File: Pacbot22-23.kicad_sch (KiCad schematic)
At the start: 8 parts, among them SW1 SW_Push, U1 ATmega32U4-A, Y1 16Mhz

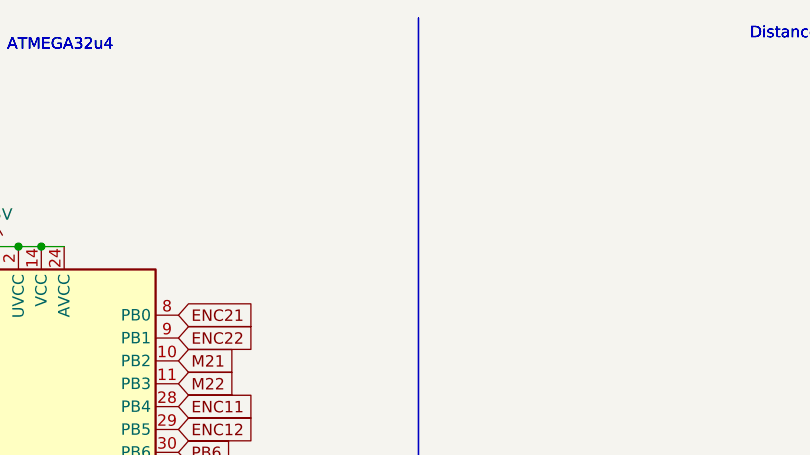
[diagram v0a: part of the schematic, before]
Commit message: Added bluetooth schematic lmao my b for not putting this on the original
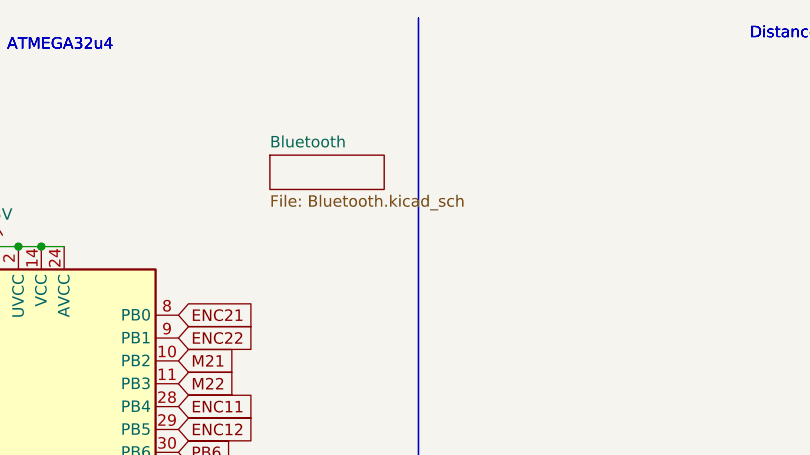
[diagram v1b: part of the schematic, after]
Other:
- added sheet Bluetooth (Bluetooth.kicad_sch)
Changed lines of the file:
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@@
+    (stroke (width 0) (type default) (color 0 0 0 0))
+  )
+  (polyline (pts (xy 176.53 71.12) (xy 234.95 71.12))
     (stroke (width 0) (type default) (color 0 0 0 0))
   )
@@
     (stroke (width 0) (type default) (color 0 0 0 0))
   )
+  (polyline (pts (xy 234.95 71.12) (xy 284.48 71.12))
+    (stroke (width 0) (type default) (color 0 0 0 0))
+  )
   (polyline (pts (xy 110.49 142.24) (xy 110.49 198.12))
     (stroke (width 0) (type default) (color 0 0 0 0))
   )
+  (polyline (pts (xy 110.49 142.24) (xy 110.49 198.12))
+    (stroke (width 0) (type default) (color 0 0 0 0))
+  )
   (polyline (pts (xy 110.49 142.24) (xy 176.53 142.24))
     (stroke (width 0) (type default) (color 0 0 0 0))
   )
+  (polyline (pts (xy 110.49 142.24) (xy 176.53 142.24))
+    (stroke (width 0) (type default) (color 0 0 0 0))
+  )
   (wire (pts (xy 78.74 93.98) (xy 85.09 93.98))
     (stroke (width 0) (type default) (color 0 0 0 0))
@@
     (stroke (width 0) (type default) (color 0 0 0 0))
   )
+  (polyline (pts (xy 176.53 113.03) (xy 284.48 113.03))
+    (stroke (width 0) (type default) (color 0 0 0 0))
+  )
   (polyline (pts (xy 88.9 142.24) (xy 110.49 142.24))
     (stroke (width 0) (type default) (color 0 0 0 0))
   )
+  (polyline (pts (xy 88.9 142.24) (xy 110.49 142.24))
+    (stroke (width 0) (type default) (color 0 0 0 0))
+  )
   (wire (pts (xy 41.91 129.54) (xy 44.45 129.54))
     (stroke (width 0) (type default) (color 0 0 0 0))
@@
     (stroke (width 0) (type default) (color 0 0 0 0))
   )
+  (polyline (pts (xy 12.7 142.24) (xy 88.9 142.24))
+    (stroke (width 0) (type default) (color 0 0 0 0))
+  )
   (wire (pts (xy 62.23 99.06) (xy 68.58 99.06))
     (stroke (width 0) (type default) (color 0 0 0 0))
@@
     (stroke (width 0) (type default) (color 0 0 0 0))
   )
+  (polyline (pts (xy 88.9 12.7) (xy 88.9 142.24))
+    (stroke (width 0) (type default) (color 0 0 0 0))
+  )
   (wire (pts (xy 16.51 50.8) (xy 16.51 55.88))
     (stroke (width 0) (type default) (color 0 0 0 0))
@@
     (stroke (width 0) (type default) (color 0 0 0 0))
   )
+  (polyline (pts (xy 176.53 142.24) (xy 176.53 166.37))
+    (stroke (width 0) (type default) (color 0 0 0 0))
+  )
   (polyline (pts (xy 12.7 181.61) (xy 50.8 181.61))
     (stroke (width 0) (type default) (color 0 0 0 0))
   )
+  (polyline (pts (xy 12.7 181.61) (xy 50.8 181.61))
+    (stroke (width 0) (type default) (color 0 0 0 0))
+  )
   (wire (pts (xy 44.45 129.54) (xy 46.99 129.54))
     (stroke (width 0) (type default) (color 0 0 0 0))
@@
     (stroke (width 0) (type default) (color 0 0 0 0))
   )
+  (polyline (pts (xy 50.8 142.24) (xy 50.8 198.12))
+    (stroke (width 0) (type default) (color 0 0 0 0))
+  )
   (polyline (pts (xy 176.53 12.7) (xy 176.53 142.24))
     (stroke (width 0) (type default) (color 0 0 0 0))
   )
+  (polyline (pts (xy 176.53 12.7) (xy 176.53 142.24))
+    (stroke (width 0) (type default) (color 0 0 0 0))
+  )
   (wire (pts (xy 44.45 38.1) (xy 46.99 38.1))
     (stroke (width 0) (type default) (color 0 0 0 0))
@@
     (effects (font (size 1.27 1.27)) (justify left bottom))
   )
+  (text "ATMEGA32u4" (at 43.18 16.51 0)
+    (effects (font (size 1.27 1.27)) (justify left bottom))
+  )
   (text "Shift Reg" (at 228.6 76.2 0)
     (effects (font (size 1.27 1.27)) (justify left bottom))
   )
+  (text "Shift Reg" (at 228.6 76.2 0)
+    (effects (font (size 1.27 1.27)) (justify left bottom))
+  )
   (text "USB Connector" (at 22.86 147.32 0)
     (effects (font (size 1.27 1.27)) (justify left bottom))
   )
+  (text "USB Connector" (at 22.86 147.32 0)
+    (effects (font (size 1.27 1.27)) (justify left bottom))
+  )
   (text "Power Term" (at 24.13 184.15 0)
     (effects (font (size 1.27 1.27)) (justify left bottom))
   )
+  (text "Power Term" (at 24.13 184.15 0)
+    (effects (font (size 1.27 1.27)) (justify left bottom))
+  )
   (text "H-Bridges" (at 227.33 115.57 0)
     (effects (font (size 1.27 1.27)) (justify left bottom))
   )
+  (text "H-Bridges" (at 227.33 115.57 0)
+    (effects (font (size 1.27 1.27)) (justify left bottom))
+  )
   (text "BNO055 IMU" (at 73.66 147.32 0)
     (effects (font (size 1.27 1.27)) (justify left bottom))
   )
+  (text "BNO055 IMU" (at 73.66 147.32 0)
+    (effects (font (size 1.27 1.27)) (justify left bottom))
+  )
   (text "Distance Sensors" (at 125.73 15.24 0)
     (effects (font (size 1.27 1.27)) (justify left bottom))
   )
+  (text "Distance Sensors" (at 125.73 15.24 0)
+    (effects (font (size 1.27 1.27)) (justify left bottom))
+  )
   (text "Decoupling Capacitors" (at 222.25 15.24 0)
+    (effects (font (size 1.27 1.27)) (justify left bottom))
+  )
+  (text "Decoupling Capacitors" (at 222.25 15.24 0)
+    (effects (font (size 1.27 1.27)) (justify left bottom))
+  )
+  (text "Motor Connectors" (at 137.16 147.32 0)
     (effects (font (size 1.27 1.27)) (justify left bottom))
   )
@@
     (pin "1")
   )
+  (sheet (at 72.39 27.94) (size 12.7 3.81) (fields_autoplaced)
+    (stroke (width 0.1524) (type solid) (color 0 0 0 0))
+    (fill (color 0 0 0 0.0000))
+    (property "Sheet name" "Bluetooth" (id 0) (at 72.39 27.2284 0)
+      (effects (font (size 1.27 1.27)) (justify left bottom))
+    )
+    (property "Sheet file" "Bluetooth.kicad_sch" (id 1) (at 72.39 32.3346 0)
+      (effects (font (size 1.27 1.27)) (justify left top))
+    )
+  )
   (sheet (at 13.97 132.08) (size 12.7 3.81) (fields_autoplaced)
     (stroke (width 0.1524) (type solid) (color 0 0 0 0))
@@
     )
   )
-  (polyline (pts (xy 176.53 71.12) (xy 234.95 71.12))
-    (stroke (width 0) (type default) (color 0 0 0 0))
-  )
-  (polyline (pts (xy 234.95 71.12) (xy 284.48 71.12))
-    (stroke (width 0) (type default) (color 0 0 0 0))
-  )
-  (polyline (pts (xy 110.49 142.24) (xy 110.49 198.12))
-    (stroke (width 0) (type default) (color 0 0 0 0))
-  )
-  (polyline (pts (xy 110.49 142.24) (xy 176.53 142.24))
-    (stroke (width 0) (type default) (color 0 0 0 0))
-  )
-  (polyline (pts (xy 176.53 113.03) (xy 284.48 113.03))
-    (stroke (width 0) (type default) (color 0 0 0 0))
-  )
-  (polyline (pts (xy 88.9 142.24) (xy 110.49 142.24))
-    (stroke (width 0) (type default) (color 0 0 0 0))
-  )
-  (polyline (pts (xy 12.7 142.24) (xy 88.9 142.24))
-    (stroke (width 0) (type default) (color 0 0 0 0))
-  )
-  (polyline (pts (xy 88.9 12.7) (xy 88.9 142.24))
-    (stroke (width 0) (type default) (color 0 0 0 0))
-  )
-  (polyline (pts (xy 176.53 142.24) (xy 176.53 166.37))
-    (stroke (width 0) (type default) (color 0 0 0 0))
-  )
-  (polyline (pts (xy 12.7 181.61) (xy 50.8 181.61))
-    (stroke (width 0) (type default) (color 0 0 0 0))
-  )
-  (polyline (pts (xy 50.8 142.24) (xy 50.8 198.12))
-    (stroke (width 0) (type default) (color 0 0 0 0))
-  )
-  (polyline (pts (xy 176.53 12.7) (xy 176.53 142.24))
-    (stroke (width 0) (type default) (color 0 0 0 0))
-  )
-  (text "ATMEGA32u4" (at 43.18 16.51 0)
-    (effects (font (size 1.27 1.27)) (justify left bottom))
-  )
-  (text "Shift Reg" (at 228.6 76.2 0)
-    (effects (font (size 1.27 1.27)) (justify left bottom))
-  )
-  (text "USB Connector" (at 22.86 147.32 0)
-    (effects (font (size 1.27 1.27)) (justify left bottom))
-  )
-  (text "Power Term" (at 24.13 184.15 0)
-    (effects (font (size 1.27 1.27)) (justify left bottom))
-  )
-  (text "H-Bridges" (at 227.33 115.57 0)
-    (effects (font (size 1.27 1.27)) (justify left bottom))
-  )
-  (text "BNO055 IMU" (at 73.66 147.32 0)
-    (effects (font (size 1.27 1.27)) (justify left bottom))
-  )
-  (text "Distance Sensors" (at 125.73 15.24 0)
-    (effects (font (size 1.27 1.27)) (justify left bottom))
-  )
-  (text "Decoupling Capacitors" (at 222.25 15.24 0)
-    (effects (font (size 1.27 1.27)) (justify left bottom))
-  )
-  (text "Motor Connectors" (at 137.16 147.32 0)
-    (effects (font (size 1.27 1.27)) (justify left bottom))
-  )
   (sheet_instances
     (path "/" (page "1"))
     (path "/590a5ee8-978b-43ec-b66a-3ea6e6e9d751" (page "2"))
+    (path "/4c040f2f-fa7f-436a-8faf-9b6a0a50ff47" (page "3"))
   )
   (symbol_instances
+    (path "/4c040f2f-fa7f-436a-8faf-9b6a0a50ff47/1235810c-b41b-4ed0-bd20-969bf45f4c5d"
+      (reference "#PWR?") (unit 1) (value "+5V") (footprint "")
+    )
     (path "/3c0a01b7-4e1b-44d8-bdba-30f1191e0e18"
       (reference "#PWR?") (unit 1) (value "GND") (footprint "")
@@
       (reference "#PWR?") (unit 1) (value "+5V") (footprint "")
     )
+    (path "/4c040f2f-fa7f-436a-8faf-9b6a0a50ff47/7fa139b8-9215-4d8d-b8f6-47bf890e7075"
+      (reference "#PWR?") (unit 1) (value "GND") (footprint "")
+    )
     (path "/7fb65cb0-26d4-43cc-a7eb-8bd5a42d0ad2"
       (reference "#PWR?") (unit 1) (value "+5V") (footprint "")
@@
       (reference "C10") (unit 1) (value "1uF") (footprint "")
     )
+    (path "/4c040f2f-fa7f-436a-8faf-9b6a0a50ff47/2f3e5db4-814e-49e7-9df2-328f7ec40bd7"
+      (reference "J?") (unit 1) (value "HC-05") (footprint "")
+    )
     (path "/c1671872-1d10-42a0-be49-f152cf9a6c5b"
       (reference "R10") (unit 1) (value "10k") (footprint "")
@@
       (reference "R20") (unit 1) (value "10k") (footprint "")
     )
+    (path "/4c040f2f-fa7f-436a-8faf-9b6a0a50ff47/71a24c17-86c0-4f2a-9098-218d0856092e"
+      (reference "R?") (unit 1) (value "100r") (footprint "")
+    )
     (path "/d23bc10b-7b30-45e0-be45-9461d6acd6cc"

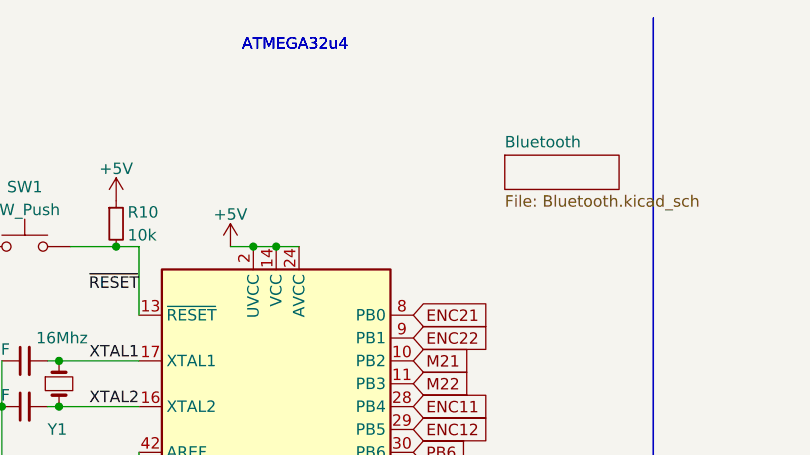
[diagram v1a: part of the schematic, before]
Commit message: Added LVR
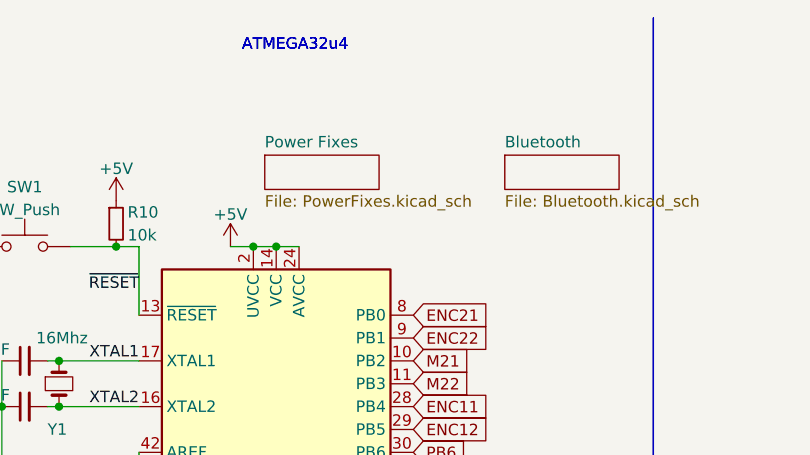
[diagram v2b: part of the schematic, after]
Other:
- added sheet Power Fixes (PowerFixes.kicad_sch)
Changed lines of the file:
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@@
     (pin "1")
+  )
+  (sheet (at 45.72 27.94) (size 12.7 3.81) (fields_autoplaced)
+    (stroke (width 0.1524) (type solid) (color 0 0 0 0))
+    (fill (color 0 0 0 0.0000))
+    (property "Sheet name" "Power Fixes" (id 0) (at 45.72 27.2284 0)
+      (effects (font (size 1.27 1.27)) (justify left bottom))
+    )
+    (property "Sheet file" "PowerFixes.kicad_sch" (id 1) (at 45.72 32.3346 0)
+      (effects (font (size 1.27 1.27)) (justify left top))
+    )
   )
   (sheet (at 72.39 27.94) (size 12.7 3.81) (fields_autoplaced)
@@
     (path "/590a5ee8-978b-43ec-b66a-3ea6e6e9d751" (page "2"))
     (path "/4c040f2f-fa7f-436a-8faf-9b6a0a50ff47" (page "3"))
+    (path "/00edbbb4-cd26-461b-b990-f87a8e329c1c" (page "4"))
   )
   (symbol_instances
@@
       (reference "#PWR?") (unit 1) (value "GND") (footprint "")
     )
+    (path "/00edbbb4-cd26-461b-b990-f87a8e329c1c/4767fd76-6b58-4859-b099-fd1c871601c5"
+      (reference "#PWR?") (unit 1) (value "+5V") (footprint "")
+    )
     (path "/583201a5-9f01-499a-806a-a1c99ed66b6c"
       (reference "#PWR?") (unit 1) (value "GND") (footprint "")
@@
     (path "/a9419ac5-56dd-48db-9f7a-b4183b1c6a1c"
       (reference "#PWR?") (unit 1) (value "GND") (footprint "")
+    )
+    (path "/00edbbb4-cd26-461b-b990-f87a8e329c1c/cfeb6c6d-8f20-41a8-a483-a658024a3995"
+      (reference "#PWR?") (unit 1) (value "+8V") (footprint "")
     )
     (path "/dbabece7-cfc2-4b30-bd49-2b0169e2eb13"
@@
       (reference "C10") (unit 1) (value "1uF") (footprint "")
     )
+    (path "/00edbbb4-cd26-461b-b990-f87a8e329c1c/3720c41d-9d7a-47a6-8680-7f74645e7d2f"
+      (reference "C?") (unit 1) (value "10uF") (footprint "")
+    )
+    (path "/00edbbb4-cd26-461b-b990-f87a8e329c1c/3df3569d-68dd-4c79-94e3-37e6758c6645"
+      (reference "C?") (unit 1) (value "22uF") (footprint "")
+    )
     (path "/4c040f2f-fa7f-436a-8faf-9b6a0a50ff47/2f3e5db4-814e-49e7-9df2-328f7ec40bd7"
       (reference "J?") (unit 1) (value "HC-05") (footprint "")
@@
       (reference "SW1") (unit 1) (value "SW_Push") (footprint "")
     )
+    (path "/00edbbb4-cd26-461b-b990-f87a8e329c1c/304bc55a-6092-48bb-96c6-a76beb166012"
+      (reference "SW?") (unit 1) (value "SW_DPDT_x2") (footprint "")
+    )
     (path "/590a5ee8-978b-43ec-b66a-3ea6e6e9d751/adc48e5e-6897-4611-a6a0-900fdafbc6eb"
       (reference "TP_5V") (unit 1) (value "TestPoint") (footprint "")
@@
       (reference "U1") (unit 1) (value "ATmega32U4-A") (footprint "Package_QFP:TQFP-44_10x10mm_P0.8mm")
     )
+    (path "/00edbbb4-cd26-461b-b990-f87a8e329c1c/425ed8e9-666a-40f8-a3f6-5951f1635e46"
+      (reference "U?") (unit 1) (value "LT1175-5_SOT223") (footprint "Package_TO_SOT_SMD:SOT-223-3_TabPin2")
+    )
     (path "/e4a0ec35-7592-44cc-8cca-728fc52023c0"

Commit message: Push bluetooth
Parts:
- added C20, C21, C22, C23, C24, C25: 0.1uF, symbol Device:C_Small
- added C26: 10uF, symbol Device:C_Small
- added IC?: SN74HCS264DR, SOIC127P600X175-14N, symbol CustomSymbols:SN74HCS264DR
- added J1, J2, J3, J4, J5, J6, J7, J8: VL6180X, symbol CustomSymbols:VL6180X
- added J10: Screw_Terminal_01x02, symbol Connector:Screw_Terminal_01x02
- added J20: USB_B_Micro, symbol Connector:USB_B_Micro
- added J30: BNO-055, symbol CustomSymbols:BNO-055
- added R1, R2: 20r, symbol Device:R_Small
- added U20, U21: L9110_HBridge, symbol CustomSymbols:L9110_HBridge
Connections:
- net +5V: now also C20.1, C21.1, C22.1, C23.1, C24.1, C25.1, C26.1, IC?.1 (A), IC?.14 (VCC), IC?.9 (~{CLR}), J1.1 (VIN), J10.1 (Pin_1), J2.1 (VIN), J20.1 (VBUS), J3.1 (VIN), J30.1 (VIN), J4.1 (VIN), J5.1 (VIN), J7.1 (VIN), J8.1 (VIN), U20.2 (VCC), U20.3 (VCC), U21.2 (VCC), U21.3 (VCC)
- net BNO_INT: now also J30.7 (INT)
- net BNO_RST: now also J30.6 (RST)
- net D+: now also R1.2
- net D-: now also R2.1
- net GND: now also C20.2, C21.2, C22.2, C23.2, C24.2, C25.2, C26.2, IC?.7 (GND), J1.2 (GND), J10.2 (Pin_2), J2.2 (GND), J20.5 (GND), J3.2 (GND), J30.3 (GND), J30.8 (ADR), J4.2 (GND), J5.2 (GND), J6.2 (GND), J7.2 (GND), J8.2 (GND), U20.5 (GND), U20.8 (GND), U21.5 (GND), U21.8 (GND)
- net M11: now also U20.6 (IA)
- net M12: now also U20.7 (IB)
- net M21: now also U21.6 (IA)
- net M22: now also U21.7 (IB)
- net SCL: now also J1.3 (SCL), J2.3 (SCL), J3.3 (SCL), J30.4 (SCL), J4.3 (SCL), J5.3 (SCL), J6.3 (SCL), J7.3 (SCL), J8.3 (SCL)
- net SDA: now also J1.4 (SDA), J2.4 (SDA), J3.4 (SDA), J30.5 (SDA), J4.4 (SDA), J5.4 (SDA), J6.4 (SDA), J7.4 (SDA), J8.4 (SDA)
- net SR_C: now also IC?.8 (CLK)
- net SR_D: now also IC?.2 (B)
- new net: J20.2 (D-), R2.2
- new net: J20.3 (D+), R1.1
- new net M1_PWR+: U20.1 (OA)
- new net M1_PWR-: U20.4 (OB)
- new net M2_PWR+: U21.1 (OA)
- new net M2_PWR-: U21.4 (OB)
- new net XS1: IC?.3 (QA), J1.6 (XSHUT)
- new net XS2: IC?.4 (QB), J2.6 (XSHUT)
- new net XS3: IC?.5 (QC), J3.6 (XSHUT)
- new net XS4: IC?.6 (QD), J4.6 (XSHUT)
- new net XS5: IC?.10 (QE), J5.6 (XSHUT)
- new net XS6: IC?.11 (QF), J6.6 (XSHUT)
- new net XS7: IC?.12 (QG), J7.6 (XSHUT)
- new net XS8: IC?.13 (QH), J8.6 (XSHUT)
- no-connect marks 0 -> 5

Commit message: Merged in everyone's schematic changes
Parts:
- added J40, J41: 6V_DC_Motor, symbol CustomSymbols:6V_DC_Motor
- gave numbers to parts that had none: 1
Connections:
- net +5V: now also J40.4 (E_PWR), J41.4 (E_PWR); no longer J10.1 (Pin_1), U20.2 (VCC), U20.3 (VCC), U21.2 (VCC), U21.3 (VCC)
- net ENC11: now also J40.5 (ENCA)
- net ENC12: now also J40.6 (ENCB)
- net ENC21: now also J41.5 (ENCA)
- net ENC22: now also J41.6 (ENCB)
- net GND: now also J40.3 (E_GND), J41.3 (E_GND)
- net M1_PWR+: now also J40.1 (M_PWR+)
- net M1_PWR-: now also J40.2 (M_PWR-)
- net M2_PWR+: now also J41.1 (M_PWR+)
- net M2_PWR-: now also J41.2 (M_PWR-)
- new net +8V: J10.1 (Pin_1), U20.2 (VCC), U20.3 (VCC), U21.2 (VCC), U21.3 (VCC)

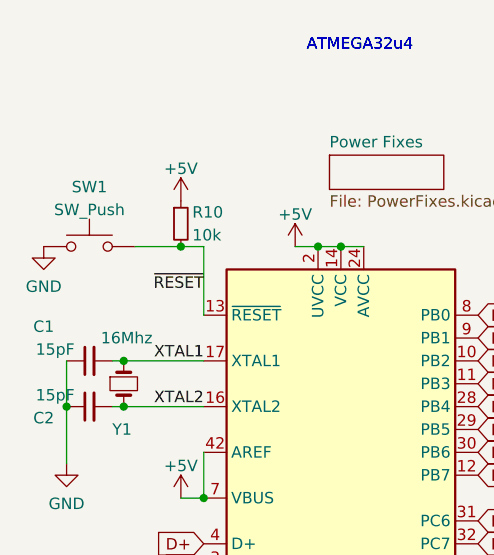
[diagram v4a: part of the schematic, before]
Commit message: Finishing touches (associating footprints) to schematic
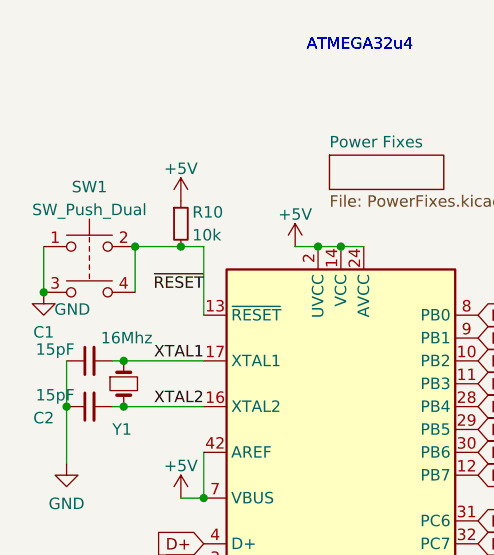
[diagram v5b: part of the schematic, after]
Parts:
- removed SW1: SW_Push, symbol Switch:SW_Push
- added SW1: SW_Push_Dual, CustomFootprints:TL3305AF260QG, symbol Switch:SW_Push_Dual
- C1, C10, C2, C20, C21, C22, C23, C24, C25, C26: footprint (none) -> Capacitor_SMD:C_0805_2012Metric
- J1, J2, J3, J4, J5, J6, J7, J8: footprint (none) -> CustomFootprints:VL6180X
- J10: footprint (none) -> Connector_PinSocket_2.54mm:PinSocket_1x02_P2.54mm_Vertical
- J20: footprint (none) -> Connector_USB:USB_Micro-B_GCT_USB3076-30-A
- J30: footprint (none) -> CustomFootprints:BNO055
- J40, J41: footprint (none) -> CustomFootprints:6V_DC_Motor
- R1, R10, R2, R20: footprint (none) -> Resistor_SMD:R_0805_2012Metric
- U10: footprint SOIC127P600X175-14N -> CustomFootprints:SOIC127P600X175-14N
- U20, U21: footprint (none) -> CustomFootprints:Adafruit_L9110_HBridge
- Y1: footprint (none) -> Crystal:Crystal_SMD_5032-2Pin_5.0x3.2mm_HandSoldering
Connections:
- net GND: now also SW1.1, SW1.3
- net ~{RESET}: now also SW1.2, SW1.4

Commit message: Pushing PCB
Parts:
- added M1: M1_Mount, CustomFootprints:Motor_Mount, symbol Connector_Generic:Conn_01x02
- added M2: M2_Mount, CustomFootprints:Motor_Mount, symbol Connector_Generic:Conn_01x02
- added R60, R61: 2k2, Resistor_SMD:R_0805_2012Metric, symbol Device:R_Small
- J10: footprint Connector_PinSocket_2.54mm:PinSocket_1x02_P2.54mm_Vertical -> CustomFootprints:POWER_TERM
- R1, R2: value 20r -> 22r
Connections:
- net +5V: now also J6.1 (VIN), R60.1, R61.1; no longer J20.1 (VBUS)
- net SCL: now also R61.2
- net SDA: now also R60.2
- new net VUSB: J20.1 (VBUS)
- no-connect marks 5 -> 9

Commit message: Changes... James Changes
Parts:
- removed J10: Screw_Terminal_01x02, CustomFootprints:POWER_TERM, symbol Connector:Screw_Terminal_01x02
- removed M1: M1_Mount, CustomFootprints:Motor_Mount, symbol Connector_Generic:Conn_01x02
- removed M2: M2_Mount, CustomFootprints:Motor_Mount, symbol Connector_Generic:Conn_01x02
- added J11, J12: Conn_01x02, CustomFootprints:POWER_TERM, symbol Connector_Generic:Conn_01x02
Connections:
- net +8V: now also J12.1 (Pin_1)
- net GND: now also J11.2 (Pin_2)
- new net +4V: J11.1 (Pin_1), J12.2 (Pin_2)
- no-connect marks 9 -> 5
